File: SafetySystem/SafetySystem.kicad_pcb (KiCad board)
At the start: 2 copper layers, 70 x 60 mm, 96 parts, among them J1 Screw_Terminal_01x02, J10 Screw_Terminal_01x02, J2 Screw_Terminal_01x02, J3 Screw_Terminal_01x02, J4 AVR-ISP-10, J5 Screw_Terminal_01x02, J6 Screw_Terminal_01x02, J7 Screw_Terminal_01x02, J8 Screw_Terminal_01x02, J9 Screw_Terminal_01x02, Q1 Q_PMOS_GSD, Q10 Q_NMOS_GSD, Q11 Q_NMOS_GSD, Q12 Q_NMOS_GSD, Q2 Q_PMOS_GSD, Q3 Q_PMOS_GSD, Q4 Q_NMOS_GSD, Q5 Q_NMOS_GSD, Q6 Q_NMOS_GSD, Q7 Q_NMOS_GSD, Q8 Q_NMOS_GSD, Q9 Q_NMOS_GSD, SW2 SW_Push, SW3 SW_Push, SW4 SW_Push, U1 ST1S10PHR, U2 MQ-8, U3 ATmega8A-AU, U4 LTV-817S, U5 LTV-817S, Y1 8Mhz

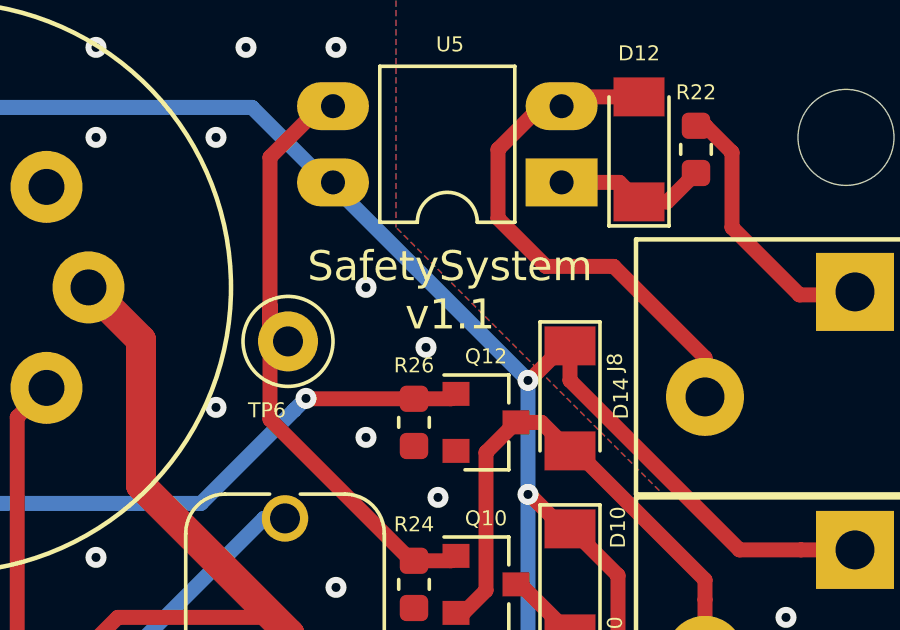
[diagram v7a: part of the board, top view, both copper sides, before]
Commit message: Changed 1.1 to 1.0 versions.
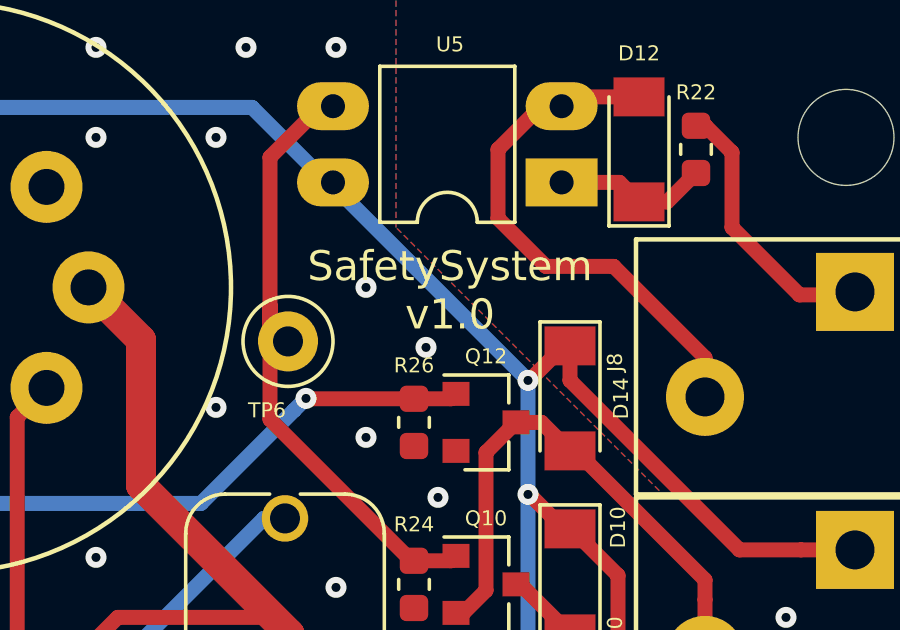
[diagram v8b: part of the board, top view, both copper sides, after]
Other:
- board text added: "SafetySystem v1.0"
- board text removed: "SafetySystem v1.1"
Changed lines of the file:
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@@
     )
   )
-  (gr_text "SafetySystem\nv1.1" (at 211.8 60.1) (layer F.SilkS)
+  (gr_text "SafetySystem\nv1.0" (at 211.8 60.1) (layer F.SilkS)
     (effects (font (size 1 1) (thickness 0.2)))
   )
